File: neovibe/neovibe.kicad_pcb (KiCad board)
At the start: 2 copper layers, 106.7 x 63.5 mm, 116 parts, among them J3 Conn_01x01, K1 Conn_01x01, M1 Conn_01x01, Q1 2N3904, Q10 2N3904, Q11 2N3904, Q12 2N3904, Q13 2N3904, Q2 2N3904, Q3 2N3904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

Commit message: more placement
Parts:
- removed R43: 4.7K, Resistor_THT:R_Axial_DIN0207_L6.3mm_D2.5mm_P7.62mm_Horizontal
- moved C5 159.8 mm to (73.7, 31.7), turned to 90 degrees
- moved C6 154.7 mm to (68.6, 40.6)
- moved C18 132.8 mm to (53.4, 59.7)
- moved R11 132.4 mm to (68.6, 26.7), turned to -90 degrees
- moved C23 130.0 mm to (57.2, 85.1)
- moved C4 126.5 mm to (62.2, 26.7), turned to -90 degrees
- moved C21 124.1 mm to (43.2, 85.1)
- moved C22 123.9 mm to (50.8, 85.1)
- moved C20 122.0 mm to (42.0, 74.9)
- moved R26 120.3 mm to (67.3, 50.8), turned to -90 degrees
- moved R25 116.9 mm to (63.5, 50.8), turned to -90 degrees
- moved R7 115.5 mm to (52.1, 25.4), turned to -90 degrees
- moved R8 113.0 mm to (48.3, 50.8), turned to 90 degrees
- moved R5 112.3 mm to (48.3, 33.0), turned to 90 degrees
- moved R6 110.8 mm to (44.5, 50.8), turned to 90 degrees
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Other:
- board size 106.7 x 63.5 mm -> 106.7 x 69.8 mm

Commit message: more placement
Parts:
- added R43: 4.7K, Resistor_THT:R_Axial_DIN0207_L6.3mm_D2.5mm_P7.62mm_Horizontal, F.Cu at (39.4, 85.1)
- moved C17 233.1 mm to (154.9, 50.8), turned to -90 degrees
- moved C26 231.8 mm to (146.1, 68.6), turned to -90 degrees
- moved C16 221.3 mm to (151.1, 43.2)
- moved Q10 211.9 mm to (162.6, 30.5), turned to 90 degrees
- moved RV2 209.6 mm to (121.7, 83.8), turned to 180 degrees
- moved C14 205.1 mm to (127.0, 43.2), turned to 180 degrees
- moved R36 204.7 mm to (161.3, 62.2), turned to 180 degrees
- moved C9 199.2 mm to (106.7, 35.5), turned to 90 degrees
- moved R30 198.3 mm to (156.2, 26.7), turned to -90 degrees
- moved R38 197.6 mm to (153.7, 69.8)
- moved R35 197.1 mm to (153.7, 58.4)
- moved C13 195.2 mm to (116.8, 43.2)
- moved K1 194.8 mm to (168.9, 82.5)
- moved J3 194.6 mm to (168.9, 78.7)
- moved R48 194.3 mm to (105.4, 81.3), turned to 180 degrees
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- renumbered C16 to C101, C100 to C16
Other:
- board size 106.7 x 69.8 mm -> 144.8 x 69.8 mm

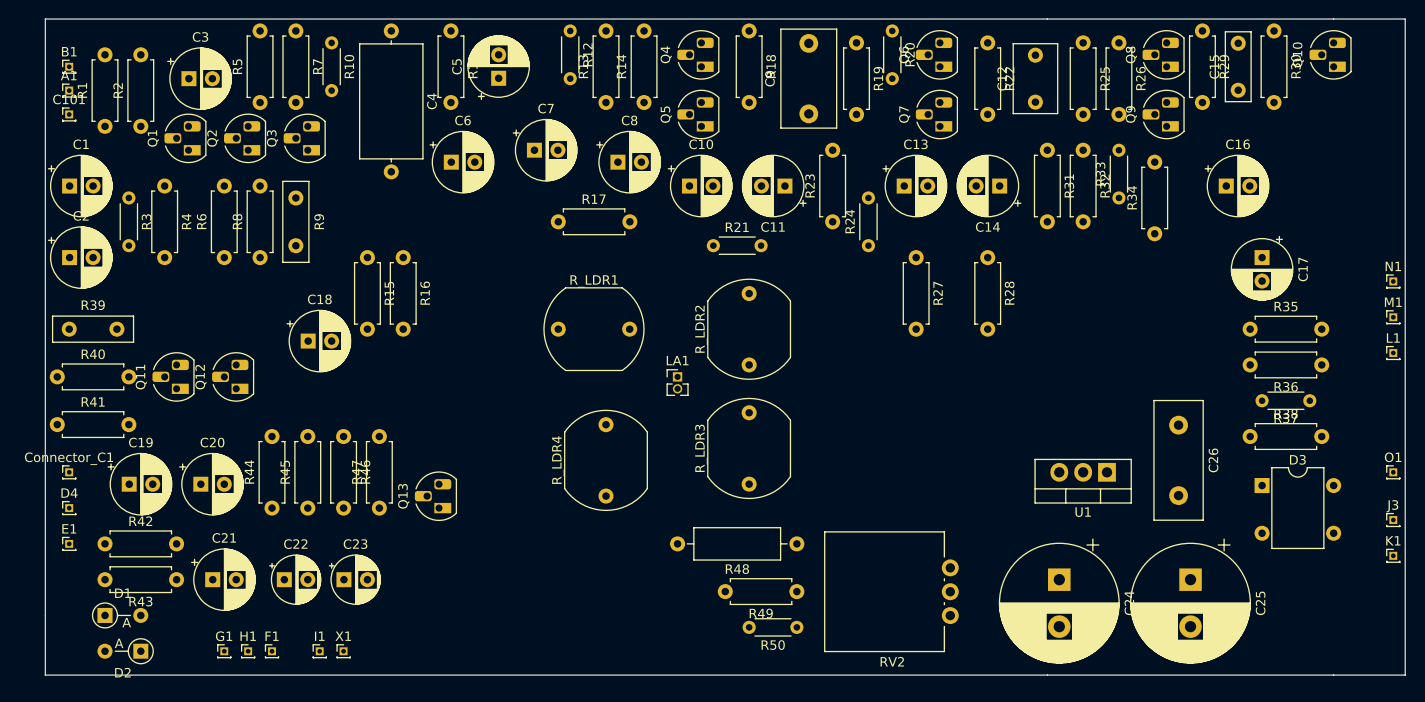
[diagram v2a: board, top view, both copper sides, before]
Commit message: 2 layer autorouted
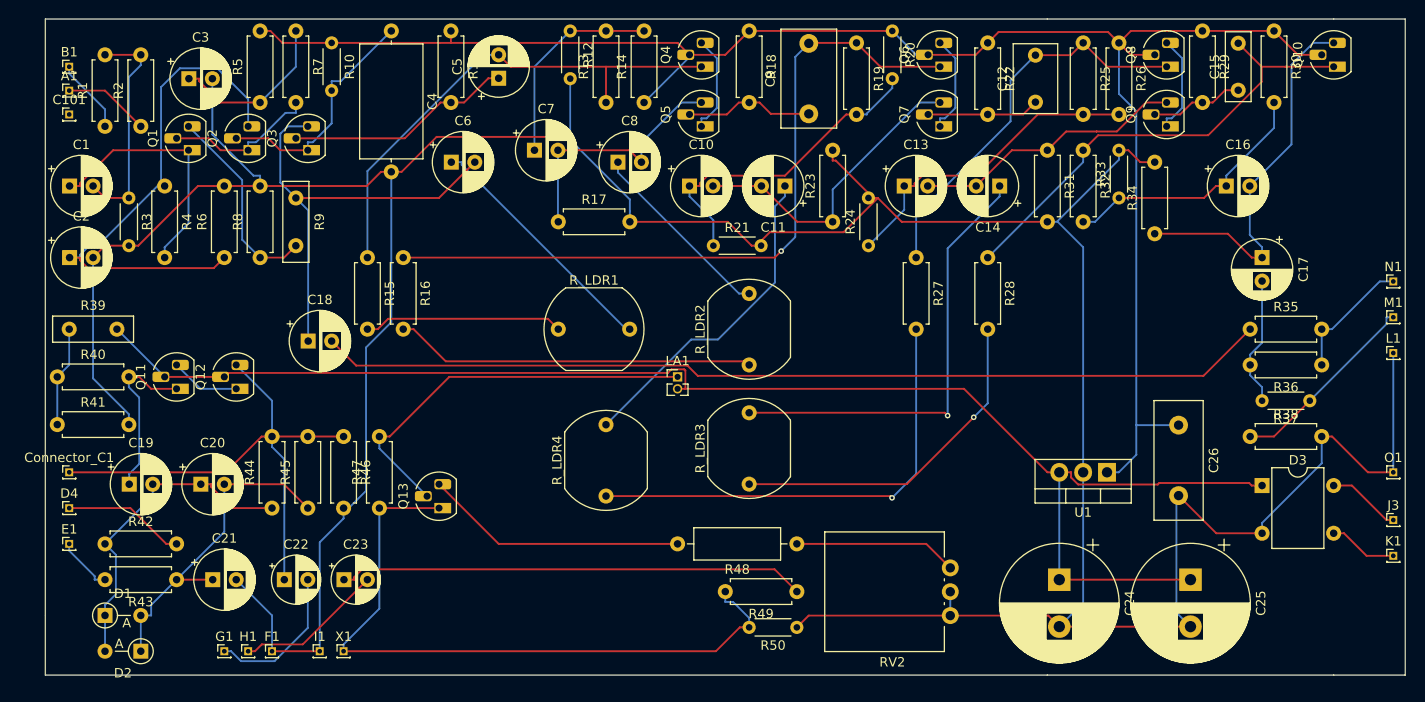
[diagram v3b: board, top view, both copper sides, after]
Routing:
- net GND: track 0.00 -> 400.0 mm, vias 0 -> 1
- net +15V: track 0.00 -> 185.0 mm
- net Net-(D3-+): track 0.00 -> 157.3 mm
- net Net-(C18-Pad2): track 0.00 -> 101.4 mm
- net Net-(Q6-B): track 0.00 -> 78.9 mm, vias 0 -> 1
- net Net-(Q13-B): track 0.00 -> 72.8 mm
- net Net-(Q2-E): track 0.00 -> 55.8 mm
- net Net-(Connector_C1-Pin_1): track 0.00 -> 55.8 mm
- net Net-(Q4-B): track 0.00 -> 54.2 mm
- net Net-(Q10-B): track 0.00 -> 50.5 mm
- net Net-(C23-Pad1): track 0.00 -> 49.8 mm
- net Net-(R27-Pad2): track 0.00 -> 49.6 mm, vias 0 -> 1
- net Net-(C14-Pad1): track 0.00 -> 48.0 mm, vias 0 -> 1
- net Net-(Q3-E): track 0.00 -> 47.2 mm
- net Net-(LA1--): track 0.00 -> 42.8 mm
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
